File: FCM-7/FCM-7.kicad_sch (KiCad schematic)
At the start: 16 parts

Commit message: cleaning up references
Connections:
- net GND: no longer CONECTOR_P5.31 (P31), CONECTOR_P5.33 (P33)
- new net PST-: CONECTOR_P5.33 (P33)
- new net PW-: CONECTOR_P5.31 (P31)

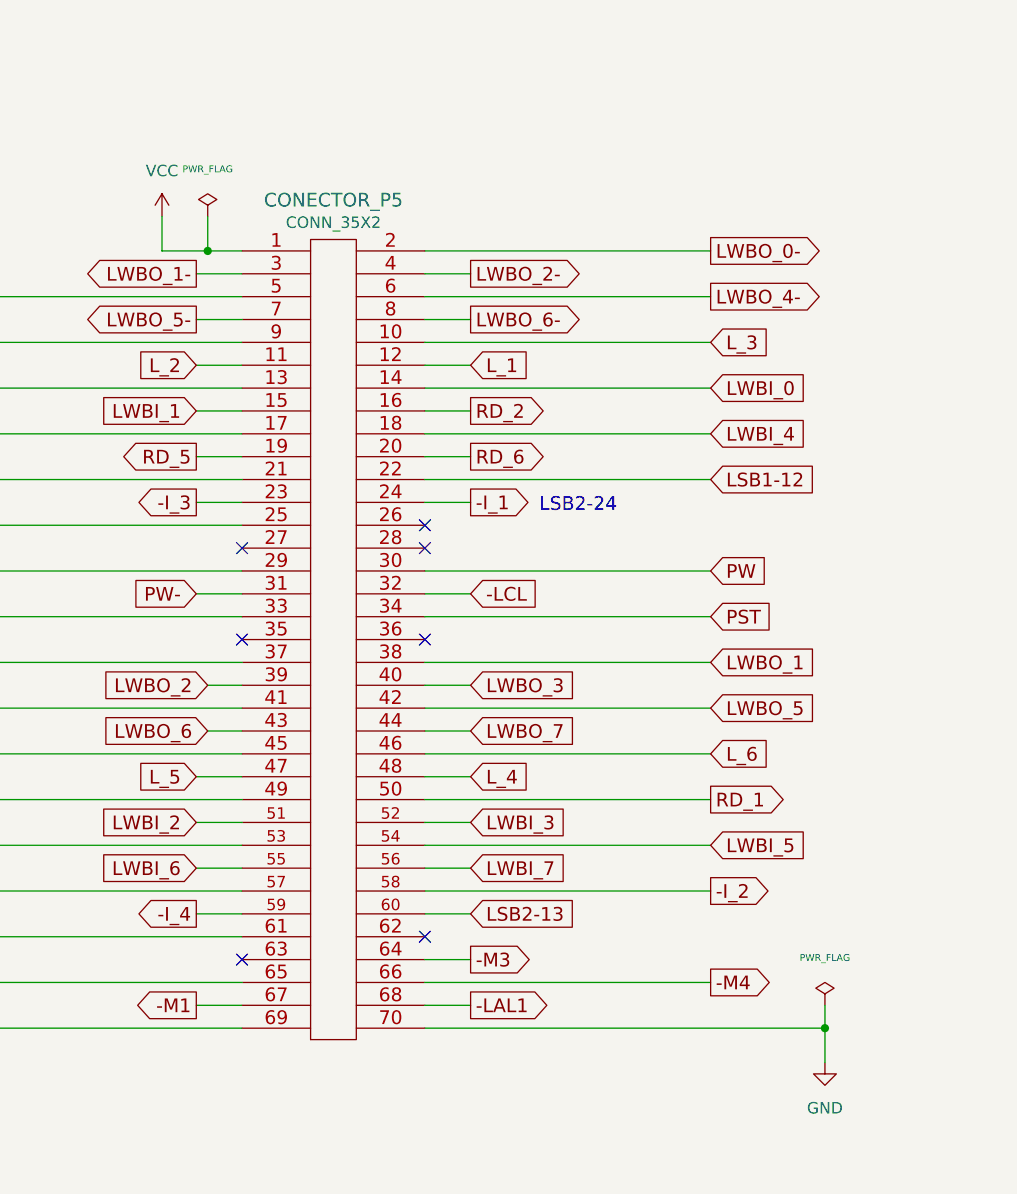
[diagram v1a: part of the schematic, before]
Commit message: Some initial fixing of ERC errors.
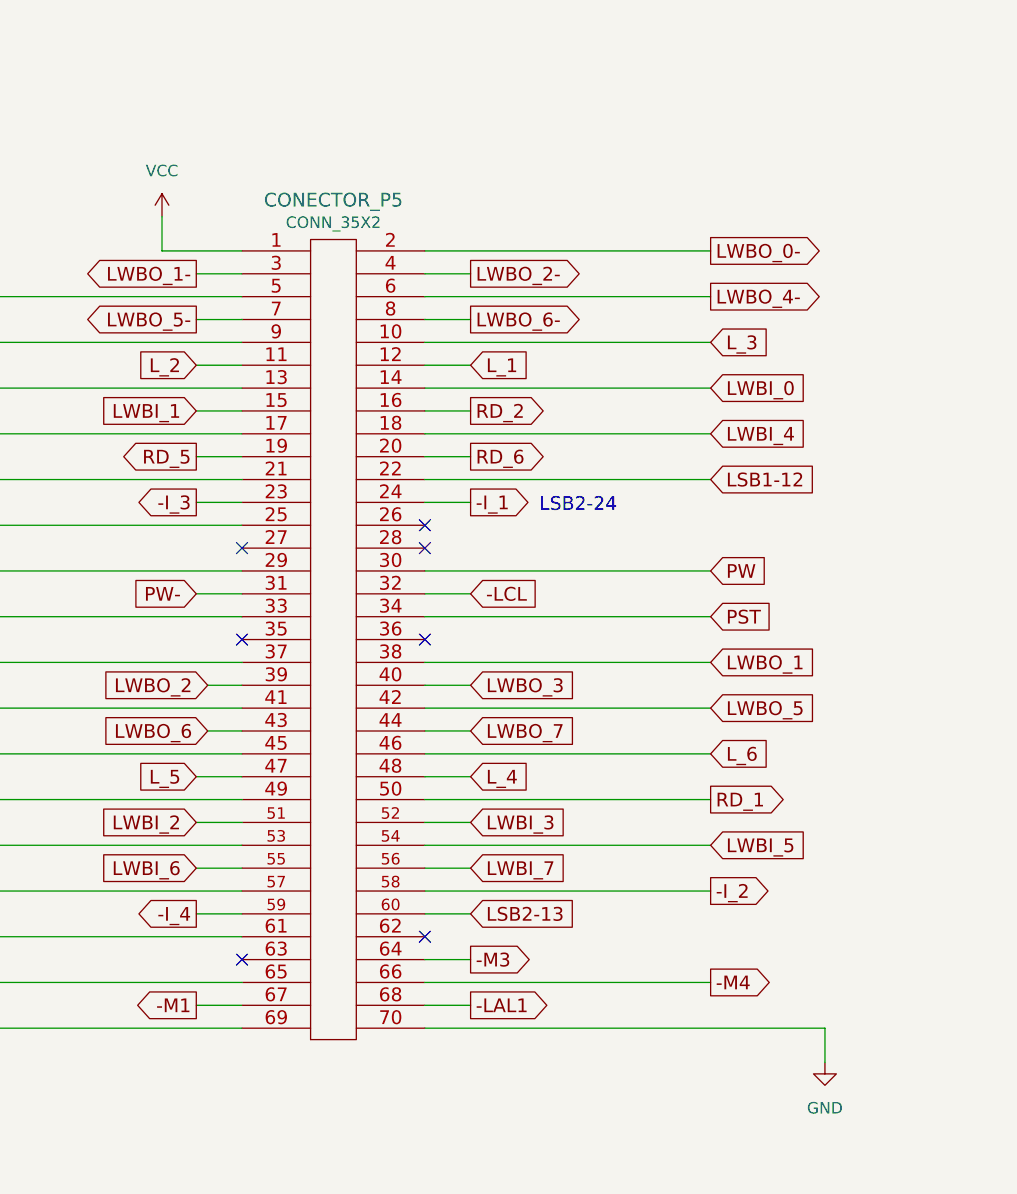
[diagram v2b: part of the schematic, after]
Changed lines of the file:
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@@
 	)
 	(junction
-		(at 77.47 78.74)
-		(diameter 0)
-		(color 0 0 0 0)
-	)
-	(junction
 		(at 224.79 119.38)
 		(diameter 0)
@@
 	)
 	(junction
-		(at 146.05 165.1)
-		(diameter 0)
-		(color 0 0 0 0)
-	)
-	(junction
 		(at 224.79 99.06)
 		(diameter 0)
@@
 	(wire
 		(pts
-			(xy 77.47 78.74) (xy 81.28 78.74)
-		)
-		(stroke
-			(width 0)
-			(type default)
-		)
-	)
-	(wire
-		(pts
 			(xy 466.09 218.44) (xy 495.3 218.44)
 		)
@@
 	(wire
 		(pts
-			(xy 146.05 162.56) (xy 146.05 165.1)
-		)
-		(stroke
-			(width 0)
-			(type default)
-		)
-	)
-	(wire
-		(pts
 			(xy 49.53 109.22) (xy 81.28 109.22)
 		)
@@
 	(wire
 		(pts
-			(xy 72.39 78.74) (xy 77.47 78.74)
+			(xy 72.39 78.74) (xy 81.28 78.74)
 		)
 		(stroke
@@
 	(wire
 		(pts
-			(xy 77.47 78.74) (xy 77.47 74.93)
-		)
-		(stroke
-			(width 0)
-			(type default)
-		)
-	)
-	(wire
-		(pts
 			(xy 72.39 78.74) (xy 72.39 74.93)
 		)
@@
 				)
 			)
-		)
-	)
-	(symbol
-		(lib_id "FCM-7-rescue:PWR_FLAG-power")
-		(at 146.05 162.56 0)
-		(unit 1)
-		(body_style 1)
-		(exclude_from_sim no)
-		(in_bom yes)
-		(on_board yes)
-		(in_pos_files yes)
-		(dnp no)
-		(property "Reference" "#FLG019"
-			(at 146.05 160.147 0)
-			(hide yes)
-			(show_name no)
-			(do_not_autoplace no)
-			(effects
-				(font
-					(size 0.762 0.762)
-				)
-			)
-		)
-		(property "Value" "PWR_FLAG"
-			(at 146.05 157.2768 0)
-			(show_name no)
-			(do_not_autoplace no)
-			(effects
-				(font
-					(size 0.762 0.762)
-				)
-			)
-		)
-		(property "Footprint" ""
-			(at 146.05 162.56 0)
-			(hide yes)
-			(show_name no)
-			(do_not_autoplace no)
-			(effects
-				(font
-					(size 1.524 1.524)
-				)
-			)
-		)
-		(property "Datasheet" ""
-			(at 146.05 162.56 0)
-			(hide yes)
-			(show_name no)
-			(do_not_autoplace no)
-			(effects
-				(font
-					(size 1.524 1.524)
-				)
-			)
-		)
-		(property "Description" ""
-			(at 146.05 162.56 0)
-			(show_name no)
-			(do_not_autoplace no)
-			(effects
-				(font
-					(size 1.27 1.27)
-				)
-			)
-		)
-		(pin "1"
-		)
-		(instances
-			(project "patinhofeio"
-				(path "/aca06203-542d-4682-a7e3-8839e24cce95/0409f498-34cc-479f-b031-007216005e3f"
-					(reference "#FLG019")
-					(unit 1)
-				)
-			)
-			(project ""
-				(path "/f891cc07-56bf-423a-bfdb-f1d90928077a"
-					(reference "#FLG019")
-					(unit 1)
-				)
-			)
-		)
-	)
-	(symbol
-		(lib_id "FCM-7-rescue:PWR_FLAG-power")
-		(at 77.47 74.93 0)
-		(unit 1)
-		(body_style 1)
-		(exclude_from_sim no)
-		(in_bom yes)
-		(on_board yes)
-		(in_pos_files yes)
-		(dnp no)
-		(property "Reference" "#FLG021"
-			(at 77.47 72.517 0)
-			(hide yes)
-			(show_name no)
-			(do_not_autoplace no)
-			(effects
-				(font
-					(size 0.762 0.762)
-				)
-			)
-		)
-		(property "Value" "PWR_FLAG"
-			(at 77.47 69.6468 0)
-			(show_name no)
-			(do_not_autoplace no)
-			(effects
-				(font
-					(size 0.762 0.762)
-				)
-			)
-		)
-		(property "Footprint" ""
-			(at 77.47 74.93 0)
-			(hide yes)
-			(show_name no)
-			(do_not_autoplace no)
-			(effects
-				(font
-					(size 1.524 1.524)
-				)
-			)
-		)
-		(property "Datasheet" ""
-			(at 77.47 74.93 0)
-			(hide yes)
-			(show_name no)
-			(do_not_autoplace no)
-			(effects
-				(font
-					(size 1.524 1.524)
-				)
-			)
-		)
-		(property "Description" ""
-			(at 77.47 74.93 0)
-			(show_name no)
-			(do_not_autoplace no)
-			(effects
-				(font
-					(size 1.27 1.27)
-				)
-			)
-		)
-		(pin "1"
-		)
-		(instances
-			(project "patinhofeio"
-				(path "/aca06203-542d-4682-a7e3-8839e24cce95/0409f498-34cc-479f-b031-007216005e3f"
-					(reference "#FLG021")
-					(unit 1)
-				)
-			)
-			(project ""
-				(path "/f891cc07-56bf-423a-bfdb-f1d90928077a"
-					(reference "#FLG021")
-					(unit 1)
-				)
-			)

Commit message: addressing a few more ERC errors
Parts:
- added unit 4 of 3B_P5
- added unit 3 of 4B_P5
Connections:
- net VCC is gone; now on net GND: 3A_P5.14 (VCC), 3A_P5.14 (VCC), 3A_P5.14 (VCC), 3A_P5.14 (VCC), 3A_P5.14 (VCC), 3A_P5.14 (VCC), 3B_P5.14 (VCC), 3B_P5.14 (VCC), 3B_P5.14 (VCC), 3B_P5.14 (VCC), 3B_P5.14 (VCC), 4B_P5.14 (VCC), 4B_P5.14 (VCC), 4B_P5.14 (VCC), 4B_P5.14 (VCC), 4B_P5.14 (VCC), 4C_P5.14 (VCC), 4C_P5.14 (VCC), 4C_P5.14 (VCC), 5A_P5.14 (VCC), 5A_P5.14 (VCC), 5A_P5.14 (VCC), 5B_P5.14 (VCC), 5B_P5.14 (VCC), 5B_P5.14 (VCC), 5B_P5.14 (VCC), 5C_P5.14 (VCC), CONECTOR_P5.1 (P1), R10_P5.1, R11_P5.1, R3_P5.1, R4_P5.1, R5_P5.1, R6_P5.1, R8_P5.1, R9_P5.1
- net GND: now also 3B_P5.14 (VCC), 3B_P5.7 (GND), 4B_P5.14 (VCC), 4B_P5.7 (GND)
- no-connect marks 7 -> 11
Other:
- moved on the sheet: 4B_P5B

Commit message: fix a whole bunch of errors
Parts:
- removed 3A_P5, 3B_P5, 4B_P5: 74LS04, symbol FCM-7-rescue:74LS04
- removed 5B_P5: 7400, symbol FCM-7-rescue:7400
- removed 5C_P5: 74LS08, symbol FCM-7-rescue:74LS08
- added 3A_P5, 3B_P5, 4B_P5: 74HC04, symbol 74xx:74HC04
- added 5B_P5, 5C_P5: 74LS08, symbol 74xx:74LS08
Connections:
- net -I_0: now also 3B_P5.5
- net -I_1: now also 4B_P5.3
- net -I_2: now also 3B_P5.13
- net -I_3: now also 3B_P5.11
- net -I_4: now also 4B_P5.1
- net -LAL1: now also 5C_P5.9
- net -LCL: now also 5B_P5.11
- net -LHC: now also 5B_P5.6
- net -M1: now also 5B_P5.13
- net -M3: now also 4B_P5.9
- net -M4: now also 5B_P5.10, 5B_P5.12, 5B_P5.4, 5B_P5.5, 5C_P5.1
- net -T70: now also 5B_P5.9
- net FN: now also 5C_P5.10
- net GND: now also 3A_P5.7 (GND), 3B_P5.7 (GND), 4B_P5.7 (GND), 5B_P5.14 (VCC), 5C_P5.14 (VCC); no longer 4C_P5.14 (VCC), 4C_P5.14 (VCC), 4C_P5.14 (VCC), 5A_P5.14 (VCC), 5A_P5.14 (VCC), 5A_P5.14 (VCC), CONECTOR_P5.1 (P1), R10_P5.1, R11_P5.1, R3_P5.1, R4_P5.1, R5_P5.1, R6_P5.1, R8_P5.1, R9_P5.1
- net LSB1-12: now also 3B_P5.6
- net LSB2-13: now also 4B_P5.4
- net LWBI_0: now also 3B_P5.2
- net LWBI_1: now also 3B_P5.4
- net LWBI_2: now also 3A_P5.4
- net LWBI_3: now also 3A_P5.6
- net LWBI_4: now also 3A_P5.2
- net LWBI_5: now also 3A_P5.8
- net LWBI_6: now also 3A_P5.10
- net LWBI_7: now also 3A_P5.12
- net PUP: now also 4B_P5.11, 5C_P5.2
- net RD_0: now also 3B_P5.1
- net RD_1: now also 3B_P5.3
- net RD_2: now also 3A_P5.3
- net RD_3: now also 3A_P5.5
- net RD_4: now also 3A_P5.1
- net RD_5: now also 3A_P5.9
- net RD_6: now also 3A_P5.11
- net RD_7: now also 3A_P5.13
- net TERRA: now also 4B_P5.13
- net at 4C_P5.9: now also 4B_P5.2
- net at 4C_P5.4: now also 3B_P5.12
- net at 4C_P5.5: now also 3B_P5.10
- net at 4C_P5.11: now also 4B_P5.12
- net at 5A_P5.1: now also 5C_P5.3
- net at 5A_P5.13: now also 5B_P5.8
- net at 5A_P5.5: now also 4B_P5.10
- net at 5A_P5.4: now also 4B_P5.8
- net at 5A_P5.3, 5A_P5.9: now also 5C_P5.8
- new net VCC: 3A_P5.14 (VCC), 3B_P5.14 (VCC), 4B_P5.14 (VCC), 4C_P5.14 (VCC), 4C_P5.14 (VCC), 4C_P5.14 (VCC), 5A_P5.14 (VCC), 5A_P5.14 (VCC), 5A_P5.14 (VCC), 5B_P5.7 (GND), 5C_P5.7 (GND), CONECTOR_P5.1 (P1), R10_P5.1, R11_P5.1, R3_P5.1, R4_P5.1, R5_P5.1, R6_P5.1, R8_P5.1, R9_P5.1
- no-connect marks 11 -> 7

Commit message: wip + PDF plot
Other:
- moved on the sheet: 3A_P5G, 3B_P5C, 3B_P5E, 3B_P5F, 3B_P5G, 4B_P5A, 4B_P5B, 4B_P5D, 4B_P5E, 4B_P5F, 4B_P5G, 4C_P5A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

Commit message: wip + PDF plot
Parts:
- removed 4C_P5, 5A_P5: 74LS11, symbol FCM-7-rescue:74LS11
- added 4C_P5, 5A_P5: 74LS11, symbol 74xx:74LS11
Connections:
- net -LCL: now also 5A_P5.2
- net GND: now also 4C_P5.14 (VCC), 5A_P5.14 (VCC)
- net LSB1-12: now also 4C_P5.3
- net LSB2-13: now also 4C_P5.10
- net PROT: now also 4C_P5.1
- net PST: now also 5A_P5.8
- net PUP: now also 4C_P5.12
- net PW: now also 5A_P5.6
- net VCC: now also 4C_P5.7 (GND), 5A_P5.7 (GND)
- net at 3B_P5.12: now also 4C_P5.4
- net at 3B_P5.10: now also 4C_P5.5
- net at 4B_P5.12: now also 4C_P5.11
- net at 4B_P5.2: now also 4C_P5.9
- net at 5C_P5.3: now also 5A_P5.1
- net at 5B_P5.8: now also 5A_P5.13
- net at 5C_P5.8: now also 5A_P5.3, 5A_P5.9
- net at 4B_P5.8: now also 5A_P5.4
- net at 4B_P5.10: now also 5A_P5.5
- new net: 4C_P5.13, 4C_P5.8
- new net: 4C_P5.2, 4C_P5.6
- new net: 5A_P5.10, 5A_P5.11, 5A_P5.12
